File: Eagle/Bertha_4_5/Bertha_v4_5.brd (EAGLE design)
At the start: 100 x 83.6 mm, 133 parts, among them CON1 JACK_DC_BARREL, CON2 JACK_DC_BARREL, IC1 MCP1703DB, IC4 DRV8811, J1 RJ12RIGHTANGLE-I2C, J2 RJ12RIGHTANGLE-I2C, Q5 BSP75, Q6 BSP75, U1 HX711, U100 RN2483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

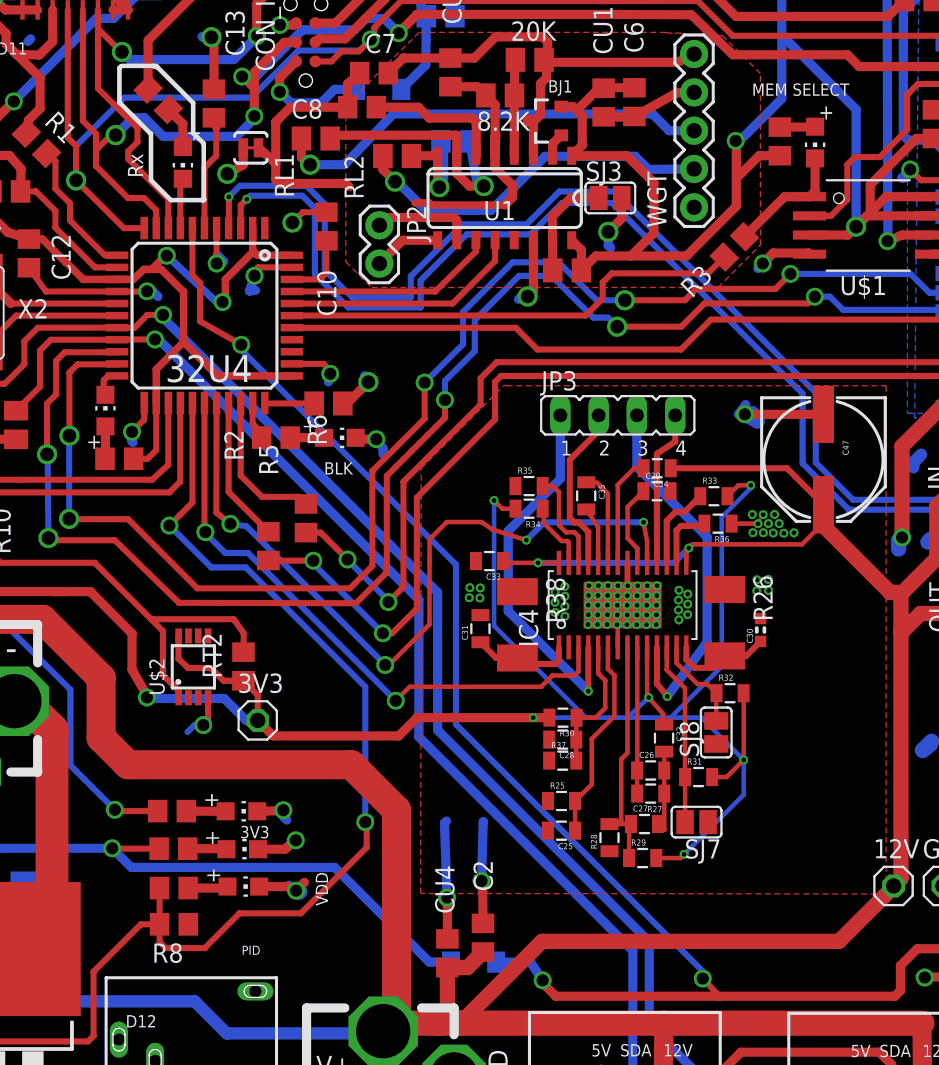
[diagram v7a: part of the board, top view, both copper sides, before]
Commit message: Corrected minor mistakes on pull uo/down lines closes #90 , Gebers to be recreated
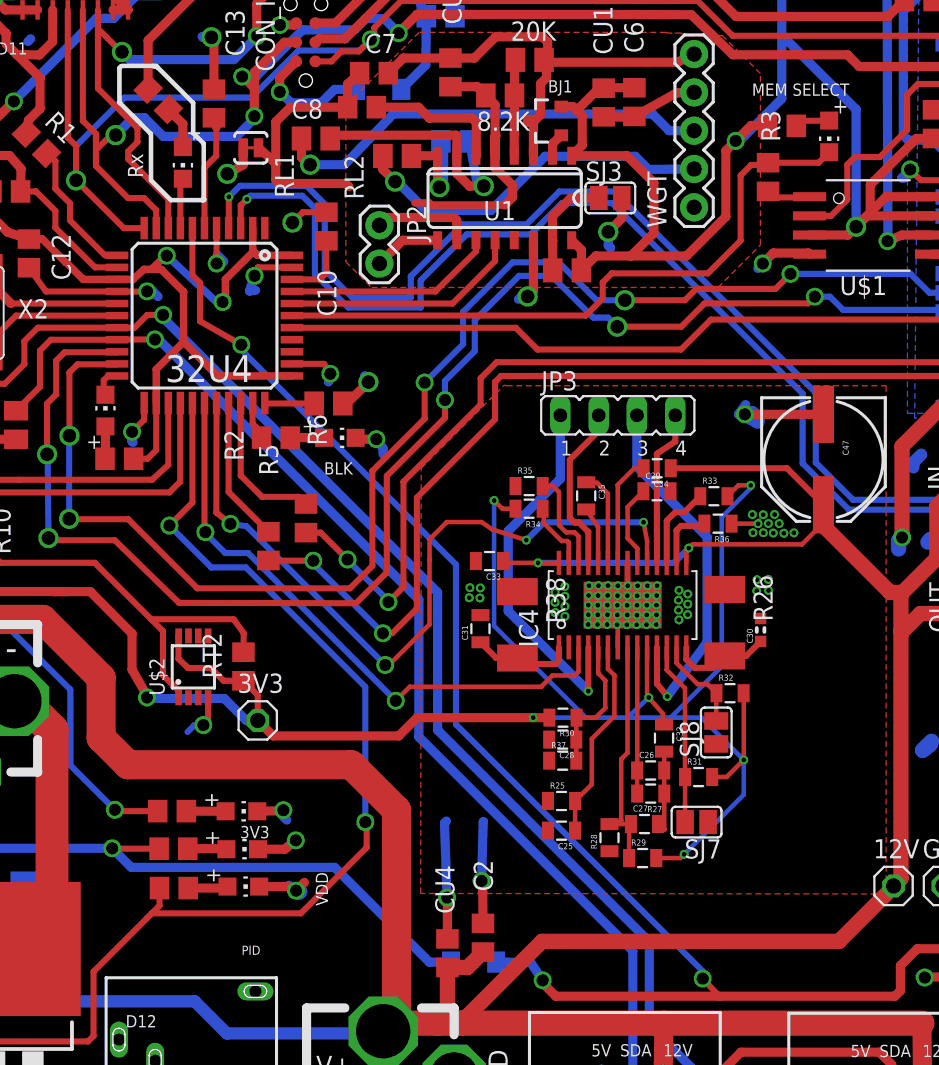
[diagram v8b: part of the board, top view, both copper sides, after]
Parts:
- removed R8: 1k, rcl:R0805
- moved R3 5.14 mm to (58.7, 65.1), turned to 90 degrees
- moved RK19 1.04 mm to (59.6, 68.5), turned to 0 degrees
- moved LDMEM 1.02 mm to (62.7, 67.8)
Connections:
- net A3: now also LDMEM.C
- net D6*: no longer R8.2
- net MEM_SEL: no longer LDMEM.C
- net N$26: no longer R8.1
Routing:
- net A3: track 30.9 -> 43.3 mm
- net MEM_SEL: track 8.10 -> 2.93 mm
- net D6*: track 81.3 -> 78.8 mm
- net 3.3V: track 575.7 -> 574.8 mm
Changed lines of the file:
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@@
 <?xml version="1.0" encoding="utf-8"?>
 <!DOCTYPE eagle SYSTEM "eagle.dtd">
-<eagle version="7.7.0">
+<eagle version="7.5.0">
 <drawing>
 <settings>
@@
 <attribute name="VALUE" x="72.116309375" y="67.46873125" size="0.8128" layer="27" rot="R90"/>
 </element>
-<element name="R3" library="rcl" package="R0805" value="1k" x="56.4504625" y="60.4662875" smashed="yes" rot="R225">
-<attribute name="NAME" x="53.641734375" y="57.009721875" size="1.27" layer="25" rot="R45"/>
-<attribute name="VALUE" x="58.2465125" y="62.2623375" size="0.8128" layer="27" rot="R45"/>
+<element name="R3" library="rcl" package="R0805" value="1k" x="58.6842875" y="65.093571875" smashed="yes" rot="R90">
+<attribute name="NAME" x="58.226196875" y="69.52380625" size="1.27" layer="25" rot="R270"/>
+<attribute name="VALUE" x="58.086546875" y="62.005446875" size="0.8128" layer="27"/>
 </element>
 <element name="RK3" library="rcl" package="R0805" value="10k" x="68.676340625" y="76.8308875" smashed="yes">
@@
 <attribute name="VALUE" x="17.702921875" y="67.895596875" size="0.8128" layer="27" rot="R270"/>
 </element>
-<element name="RK19" library="rcl" package="R0805" value="1k" x="59.464703125" y="67.4593625" smashed="yes" rot="R90">
-<attribute name="VALUE" x="59.802565625" y="70.19068125" size="0.8128" layer="27" rot="R90"/>
+<element name="RK19" library="rcl" package="R0805" value="1k" x="59.605359375" y="68.488196875" smashed="yes">
+<attribute name="VALUE" x="59.440709375" y="69.9693875" size="0.8128" layer="27"/>
 </element>
-<element name="LDMEM" library="adafruit" package="CHIP-LED0805" value="Flash" x="61.800271875" y="67.382353125" smashed="yes" rot="R180">
-<attribute name="VALUE" x="63.47281875" y="70.802140625" size="0.8128" layer="27" rot="R270"/>
+<element name="LDMEM" library="adafruit" package="CHIP-LED0805" value="Flash" x="62.73368125" y="67.789246875" smashed="yes" rot="R180">
+<attribute name="VALUE" x="64.406228125" y="71.209034375" size="0.8128" layer="27" rot="R270"/>
 </element>
 <element name="C5" library="rcl" package="C0805" value="100n" x="72.11429375" y="63.936696875" smashed="yes" rot="R270">
@@
 <attribute name="VALUE" x="18.344796875" y="1.675675" size="1.27" layer="28" rot="MR0"/>
 </element>
-<element name="R8" library="rcl" package="R0805" value="1k" x="19.288671875" y="15.544946875" rot="R180"/>
 </elements>
 <signals>
@@
 <wire x1="27.1147125" y1="55.9076125" x2="27.193240625" y2="55.91283125" width="0.4064" layer="1"/>
 <contactref element="R3" pad="2"/>
-<wire x1="55.778709375" y1="59.794534375" x2="54.693375" y2="58.7092" width="0.4064" layer="1"/>
 <wire x1="54.693375" y1="58.7092" x2="48.32045" y2="58.7092" width="0.4064" layer="1"/>
 <wire x1="27.193240625" y1="55.91283125" x2="46.593709375" y2="55.91283125" width="0.4064" layer="1"/>
@@
 <wire x1="47.7181875" y1="58.1069375" x2="47.7181875" y2="57.037309375" width="0.4064" layer="1"/>
 <wire x1="47.7181875" y1="57.037309375" x2="46.593709375" y2="55.91283125" width="0.4064" layer="1"/>
+<contactref element="LDMEM" pad="C"/>
+<wire x1="56.862259375" y1="65.197859375" x2="56.862259375" y2="60.878084375" width="0.4064" layer="1"/>
+<wire x1="56.862259375" y1="60.878084375" x2="54.693375" y2="58.7092" width="0.4064" layer="1"/>
+<wire x1="56.862259375" y1="65.197859375" x2="57.560321875" y2="65.895921875" width="0.4064" layer="1"/>
+<wire x1="57.560321875" y1="65.895921875" x2="58.5366375" y2="65.895921875" width="0.4064" layer="1"/>
+<wire x1="58.5366375" y1="65.895921875" x2="58.6842875" y2="66.043571875" width="0.4064" layer="1"/>
+<wire x1="62.73368125" y1="66.739246875" x2="62.03800625" y2="66.043571875" width="0.4064" layer="1"/>
+<wire x1="62.03800625" y1="66.043571875" x2="58.6842875" y2="66.043571875" width="0.4064" layer="1"/>
 </signal>
 <signal name="A4">
@@
 <wire x1="13.95825" y1="8.145034375" x2="13.95825" y2="12.41010625" width="0.4064" layer="1"/>
 <contactref element="RK14" pad="2"/>
-<contactref element="R8" pad="2"/>
 <wire x1="18.33185625" y1="17.94956875" x2="18.338671875" y2="17.94956875" width="0.4064" layer="1"/>
-<wire x1="18.338671875" y1="17.94956875" x2="18.338671875" y2="15.544946875" width="0.4064" layer="1"/>
-<wire x1="13.95825" y1="12.41010625" x2="17.093090625" y2="15.544946875" width="0.4064" layer="1"/>
-<wire x1="17.093090625" y1="15.544946875" x2="18.338671875" y2="15.544946875" width="0.4064" layer="1"/>
-<wire x1="18.338671875" y1="15.544946875" x2="18.338671875" y2="14.363828125" width="0.4064" layer="1"/>
-<wire x1="18.338671875" y1="14.363828125" x2="18.7325" y2="13.97" width="0.4064" layer="1"/>
-<wire x1="18.7325" y1="13.97" x2="21.328075" y2="13.97" width="0.4064" layer="1"/>
-<wire x1="21.328075" y1="13.97" x2="23.632875" y2="16.2748" width="0.4064" layer="1"/>
-<wire x1="23.632875" y1="16.2748" x2="27.7048" y2="16.2748" width="0.4064" layer="1"/>
+<wire x1="13.95825" y1="12.41010625" x2="17.509796875" y2="15.961653125" width="0.4064" layer="1"/>
+<wire x1="17.509796875" y1="15.961653125" x2="17.82294375" y2="16.2748" width="0.4064" layer="1"/>
 <wire x1="27.7048" y1="16.2748" x2="32.0675" y2="20.6375" width="0.4064" layer="1"/>
 <wire x1="32.0675" y1="22.234925" x2="31.97645625" y2="22.32596875" width="0.4064" layer="1"/>
@@
 <wire x1="21.76306875" y1="39.2099375" x2="18.986525" y2="41.98648125" width="0.4064" layer="16"/>
 <wire x1="32.0675" y1="20.6375" x2="32.0675" y2="22.234925" width="0.4064" layer="1"/>
+<wire x1="27.7048" y1="16.2748" x2="17.82294375" y2="16.2748" width="0.4064" layer="1"/>
+<wire x1="18.33185625" y1="17.94956875" x2="18.33185625" y2="16.7837125" width="0.4064" layer="1"/>
+<wire x1="18.33185625" y1="16.7837125" x2="17.82294375" y2="16.2748" width="0.4064" layer="1"/>
 </signal>
 <signal name="D10*">
@@
 <wire x1="53.277071875" y1="59.8626875" x2="49.58965625" y2="59.8626875" width="0.6096" layer="1"/>
 <wire x1="49.58965625" y1="59.8626875" x2="47.259053125" y2="59.8626875" width="0.6096" layer="1"/>
-<wire x1="56.578546875" y1="63.1641625" x2="53.277071875" y2="59.8626875" width="0.6096" layer="1"/>
 <wire x1="51.112853125" y1="64.7150125" x2="51.112853125" y2="61.385884375" width="0.6096" layer="1"/>
 <wire x1="51.112853125" y1="61.385884375" x2="49.58965625" y2="59.8626875" width="0.6096" layer="1"/>
@@
 <wire x1="71.66429375" y1="62.536696875" x2="72.11429375" y2="62.986696875" width="0.4064" layer="1" curve="90"/>
 <wire x1="77.341734375" y1="63.255175" x2="77.442096875" y2="63.3555375" width="0.6096" layer="1"/>
-<wire x1="56.578546875" y1="65.0037125" x2="56.578546875" y2="67.448628125" width="0.6096" layer="1"/>
 <wire x1="56.578546875" y1="67.448628125" x2="56.534871875" y2="67.492303125" width="0.6096" layer="1"/>
 <wire x1="56.534871875" y1="67.492303125" x2="56.7904125" y2="67.492303125" width="0.6096" layer="16"/>
 <wire x1="56.7904125" y1="67.492303125" x2="59.591234375" y2="70.293125" width="0.6096" layer="16"/>
-<wire x1="59.464703125" y1="66.5093625" x2="58.084196875" y2="66.5093625" width="0.6096" layer="1"/>
-<wire x1="58.084196875" y1="66.5093625" x2="56.578546875" y2="65.0037125" width="0.6096" layer="1"/>
-<wire x1="56.578546875" y1="65.0037125" x2="56.578546875" y2="63.1641625" width="0.6096" layer="1"/>
 <contactref element="U$2" pad="8"/>
 <wire x1="20.0952625" y1="32.67880625" x2="19.589753125" y2="33.144575" width="0.4064" layer="1"/>
@@
 <wire x1="2.68780625" y1="-1.4120125" x2="14.056903125" y2="-1.4120125" width="0.4064" layer="16"/>
 <wire x1="14.056903125" y1="-1.4120125" x2="15.728528125" y2="0.2596125" width="0.4064" layer="16"/>
+<wire x1="53.277071875" y1="59.8626875" x2="55.88496875" y2="62.470584375" width="0.6096" layer="1"/>
+<wire x1="55.88496875" y1="62.470584375" x2="55.88496875" y2="66.8424" width="0.6096" layer="1"/>
+<wire x1="55.88496875" y1="66.8424" x2="56.534871875" y2="67.492303125" width="0.6096" layer="1"/>
+<wire x1="58.655359375" y1="68.488196875" x2="57.5547" y2="68.51213125" width="0.6096" layer="1"/>
+<wire x1="57.5547" y1="68.51213125" x2="56.534871875" y2="67.492303125" width="0.6096" layer="1"/>
 </signal>
 <signal name="SDA">
@@
 <contactref element="RK19" pad="2"/>
 <contactref element="LDMEM" pad="A"/>
-<wire x1="59.464703125" y1="68.4093625" x2="61.77728125" y2="68.4093625" width="0.6096" layer="1"/>
-<wire x1="61.77728125" y1="68.4093625" x2="61.800271875" y2="68.432353125" width="0.6096" layer="1"/>
+<wire x1="62.73368125" y1="68.839246875" x2="60.76280625" y2="68.8153125" width="0.4064" layer="1"/>
+<wire x1="60.76280625" y1="68.8153125" x2="60.555359375" y2="68.488196875" width="0.4064" layer="1"/>
 </signal>
 <signal name="N$26" class="1">
@@
 <wire x1="20.23185625" y1="17.94956875" x2="22.7404875" y2="17.94956875" width="0.6096" layer="1"/>
 <wire x1="22.7404875" y1="17.94956875" x2="22.840096875" y2="18.049178125" width="0.6096" layer="1"/>
-<contactref element="R8" pad="1"/>
-<wire x1="20.238671875" y1="15.544946875" x2="20.23185625" y2="17.94956875" width="0" layer="19" extent="1-1"/>
 </signal>
 <signal name="N$27">
@@
 </signal>
 <signal name="MEM_SEL">
-<contactref element="LDMEM" pad="C"/>
 <contactref element="R3" pad="1"/>
 <contactref element="U$1" pad="CE"/>
-<wire x1="61.43514375" y1="63.7908" x2="59.774975" y2="63.7908" width="0.6096" layer="1"/>
-<wire x1="59.774975" y1="63.7908" x2="57.1222125" y2="61.1380375" width="0.6096" layer="1"/>
-<wire x1="61.800271875" y1="66.332353125" x2="61.800271875" y2="64.155928125" width="0.6096" layer="1"/>
-<wire x1="61.800271875" y1="64.155928125" x2="61.43514375" y2="63.7908" width="0.6096" layer="1"/>
+<wire x1="61.43514375" y1="63.7908" x2="60.66588125" y2="63.740946875" width="0.4064" layer="1"/>
+<wire x1="60.66588125" y1="63.740946875" x2="59.05419375" y2="63.7446875" width="0.4064" layer="1"/>
+<wire x1="59.05419375" y1="63.7446875" x2="58.6842875" y2="64.143571875" width="0.4064" layer="1"/>
 </signal>
 <signal name="N$4">
